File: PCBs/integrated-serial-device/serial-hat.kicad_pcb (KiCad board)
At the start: 2 copper layers, 193 x 113 mm, 28 parts, among them CN1 Modem port, CN2 Modem out 3, CN3 Printer port, J1 Rpi headers, K1 Quicktake, K2 ImageWriter, SW1 Modem To Proxy, SW2 Modem to Quicktake, SW3 Modem out 3, SW4 Printer out 3, SW5 Printer to Proxy, SW6 Printer to ImageWriter, U1 MAX3232

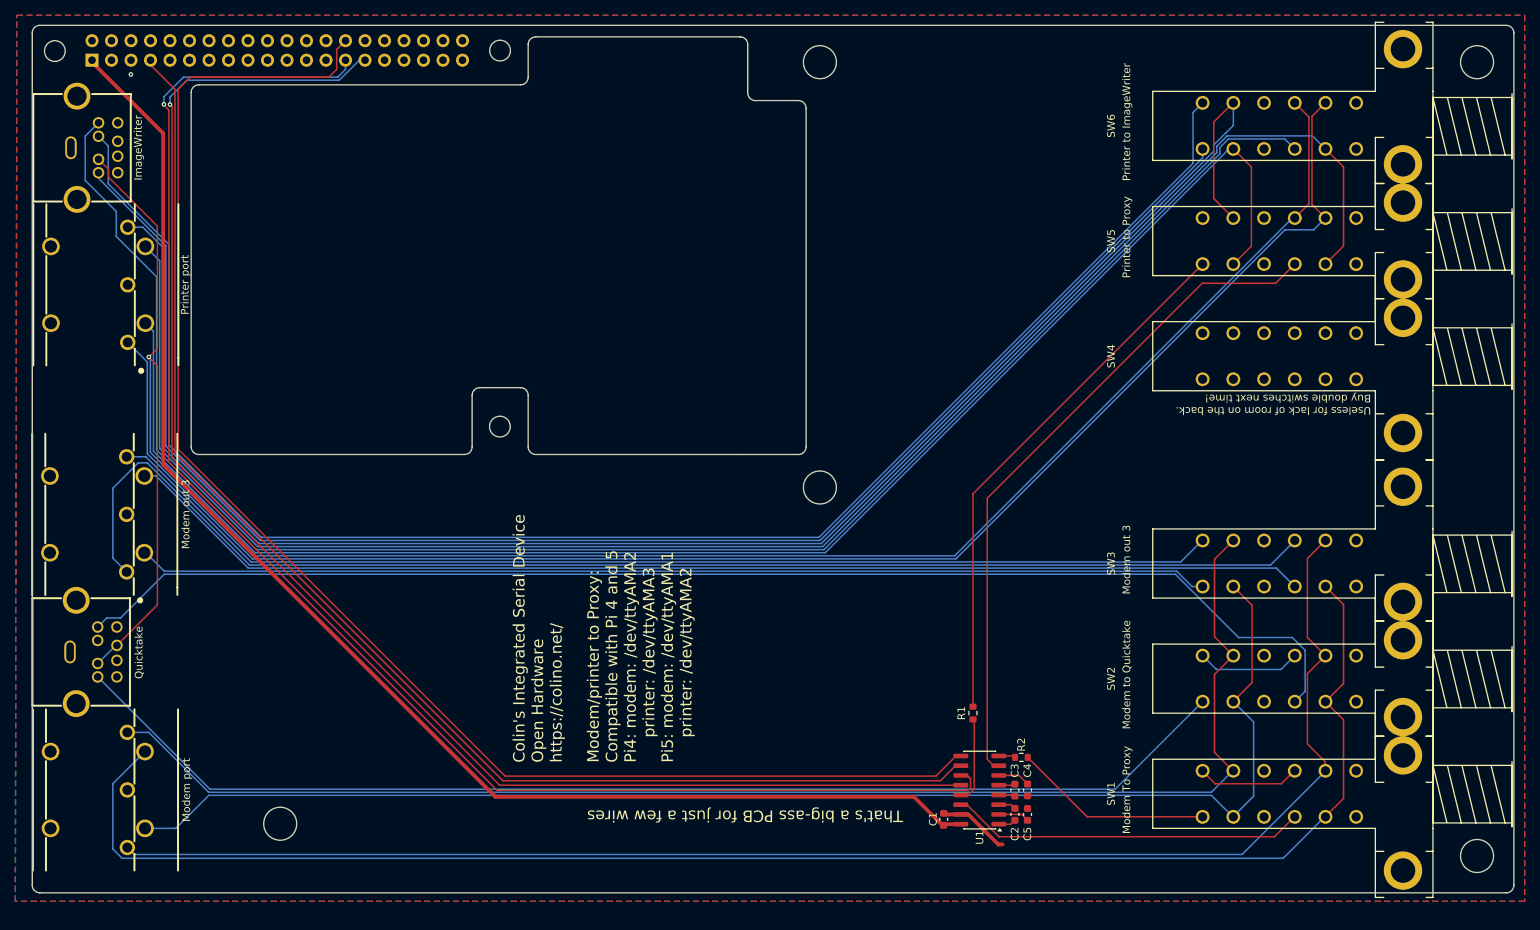
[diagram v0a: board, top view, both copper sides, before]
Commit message: Add jumper for IIc/IIgs
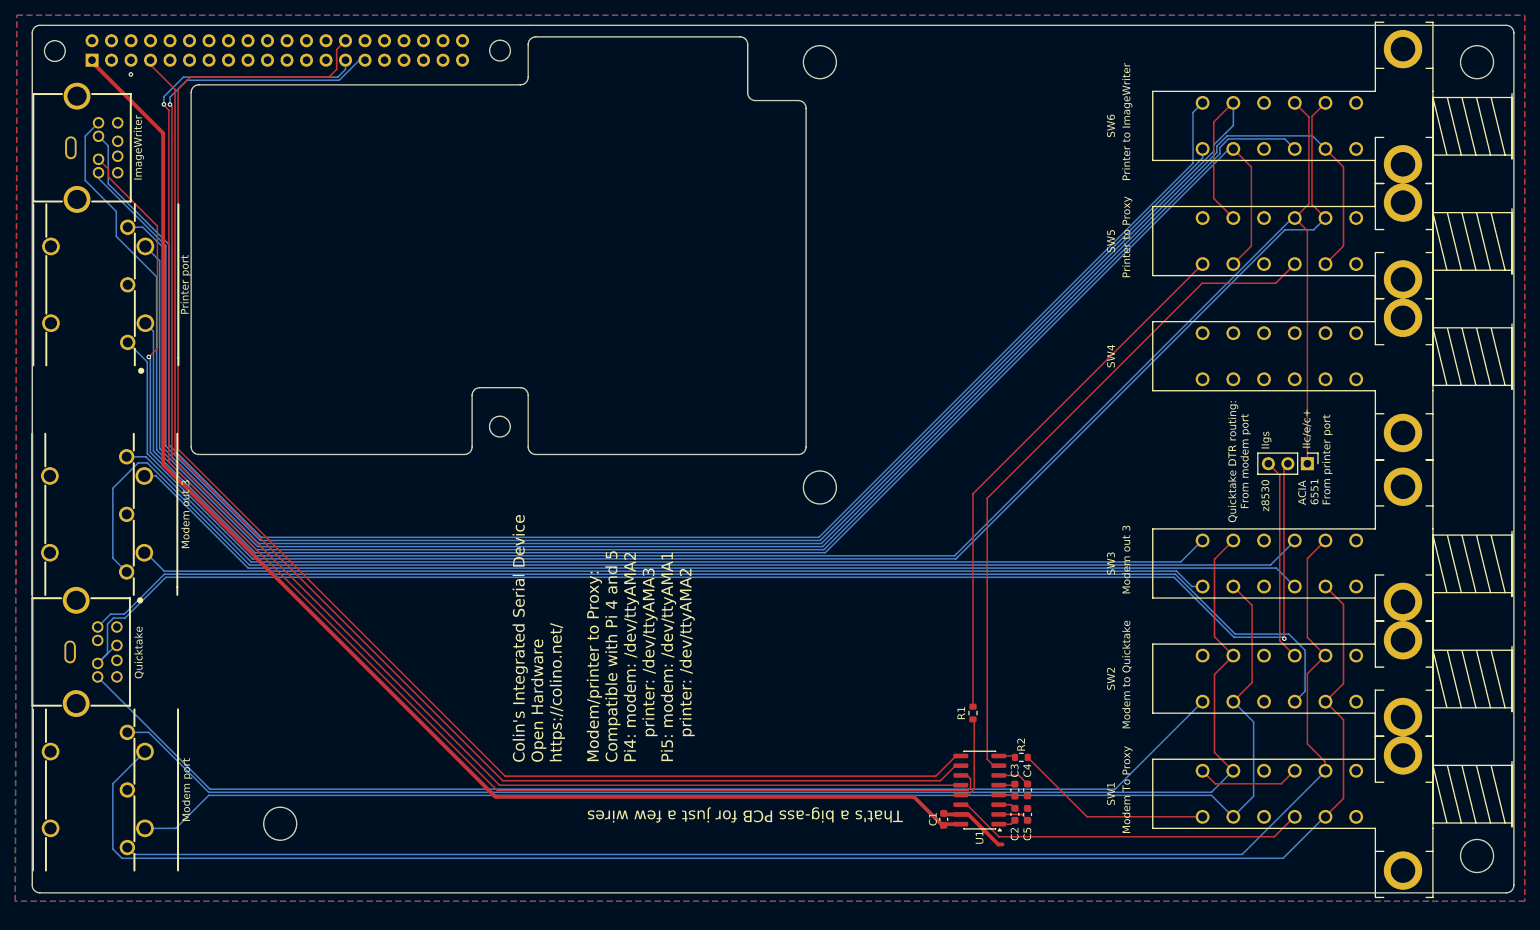
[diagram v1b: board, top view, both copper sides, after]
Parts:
- added J2: Conn_01x03_Pin, Connector_PinHeader_2.54mm:PinHeader_1x03_P2.54mm_Vertical, F.Cu at (219.9, 95.8)
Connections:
- K2 pad 1: Quicktake_DTR -> IW_DTR
- SW2 pad C1: Net-(SW2-PadC1) -> unconnected-(SW2-PadC1)
- SW2 pad D1: Net-(SW2-PadC1) -> Quicktake_DTR_Modem
- SW5 pad D1: Quicktake_DTR -> IW_DTR
- SW6 pad D1: Quicktake_DTR -> IW_DTR
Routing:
- net IW_DTR: track 0.00 -> 264.2 mm, vias 0 -> 1
- net Quicktake_DTR: track 275.2 -> 191.8 mm
- net Quicktake_DTR_Modem: track 0.00 -> 26.4 mm
- net Net-(SW2-PadC1): track 13.5 -> 0.00 mm
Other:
- board text added: "ACIA 6551"
- board text added: "From printer port"
- board text added: "IIc/e/c+"
- board text added: "IIgs"
- board text added: "Quicktake DTR routing: From modem port"
- board text added: "z8530"
- board text removed: "Useless for lack of room on the back. Buy double switches next time!"

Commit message: Add enclosures
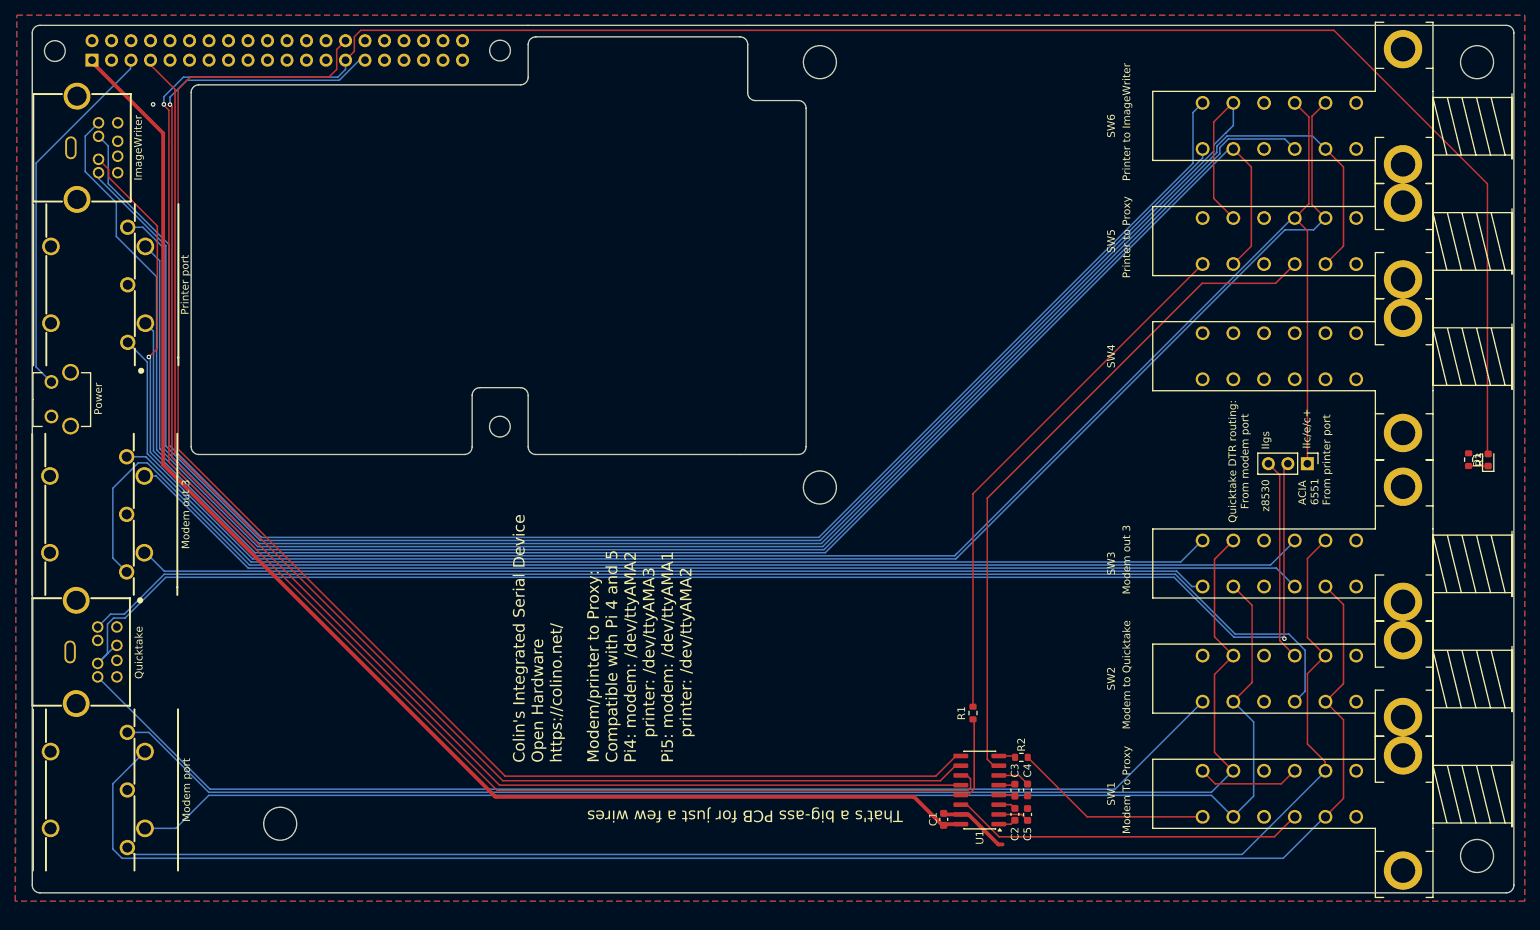
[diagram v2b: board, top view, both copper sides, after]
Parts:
- added D1: LED, LED_SMD:LED_0603_1608Metric, F.Cu at (243.4, 95.3)
- added R3: 100, Resistor_SMD:R_0603_1608Metric, F.Cu at (240.9, 95.3)
- added SW7: SW_SPST, DIN5:SPST_power_switch, F.Cu at (58.9, 87.5)
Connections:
- net TX0_out_GPIO0 renamed PWR_LED
- J1 pad 5: unconnected-(J1-Pin_5-Pad5) -> PWR_BTN
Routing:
- net PWR_LED: track 199.1 -> 394.1 mm
- net PWR_BTN: track 0.00 -> 47.9 mm
- net Net-(D1-K): track 0.00 -> 2.55 mm
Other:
- board text added: "Power"

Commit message: Add fan headers
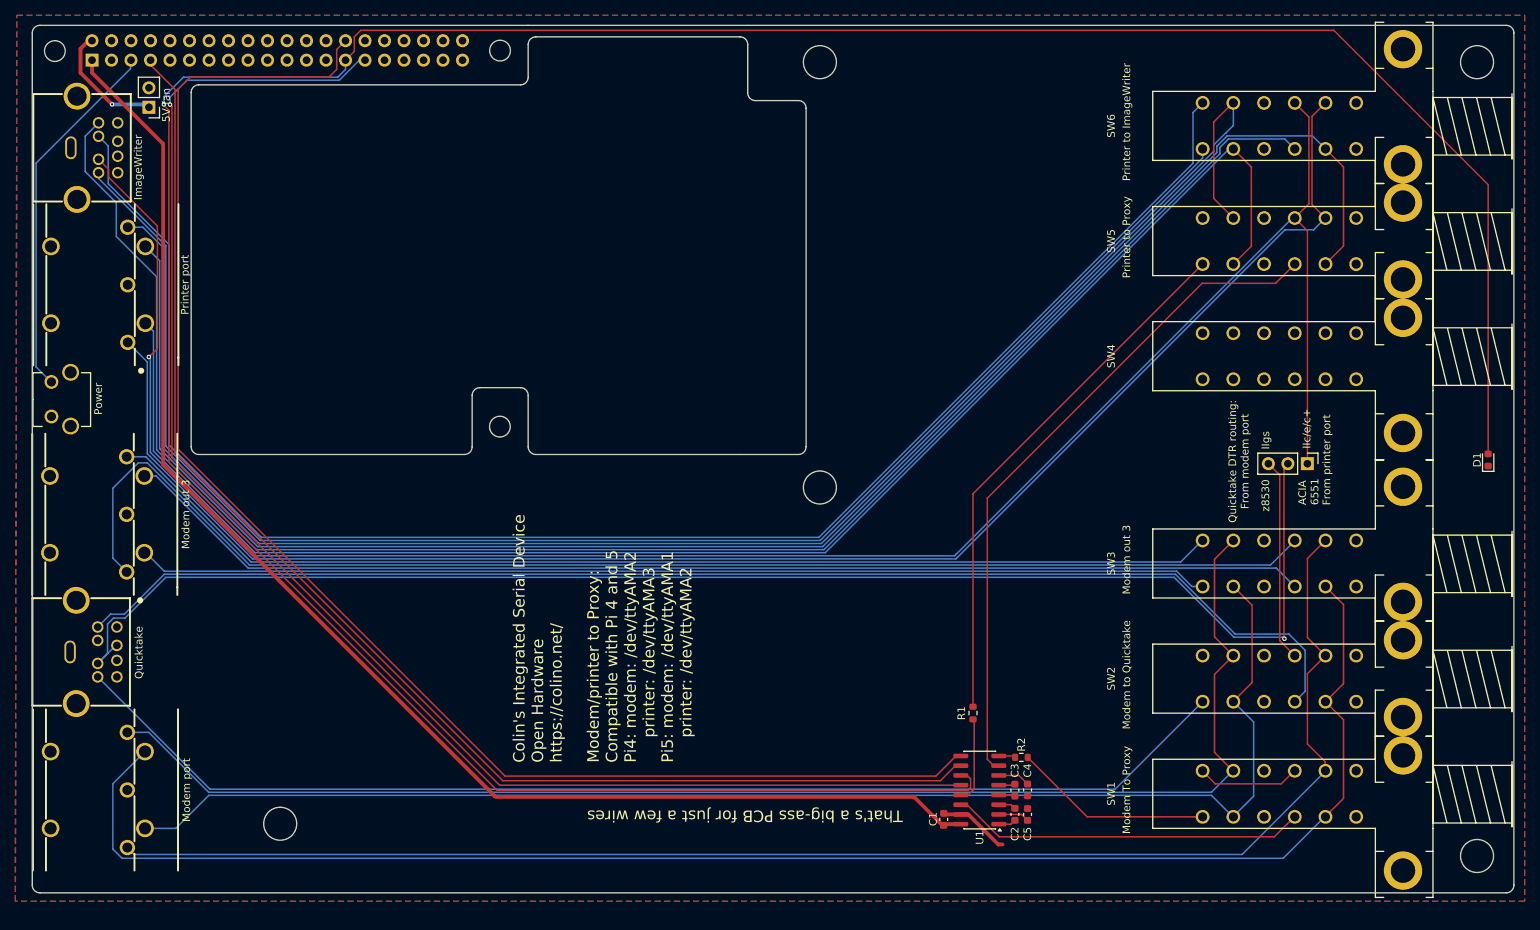
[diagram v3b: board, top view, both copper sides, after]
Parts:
- removed R3: 100, Resistor_SMD:R_0603_1608Metric
- added J3: Conn_01x02_Pin, Connector_PinHeader_2.54mm:PinHeader_1x02_P2.54mm_Vertical, F.Cu at (69.0, 49.4)
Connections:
- D1 pad 1: Net-(D1-K) -> GND
- J1 pad 2: unconnected-(J1-Pin_2-Pad2) -> 5V
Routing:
- net 5V: track 0.00 -> 15.8 mm, vias 0 -> 1
- net Net-(D1-K): track 2.55 -> 0.00 mm
- net GND: vias 1 -> 0
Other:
- board text added: "5V fan"

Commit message: CISD ready
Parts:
- removed R1, R2: 3.3k, Resistor_SMD:R_0603_1608Metric
- moved J3 2.68 mm to (69.0, 46.7), turned to 0 degrees
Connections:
- U1 pad 13: Net-(U1-R1IN) -> A2_AUX_TTY_TX
- U1 pad 8: Net-(U1-R2IN) -> A2_TTY_TX
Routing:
- net A2_AUX_TTY_TX: track 70.2 -> 82.8 mm
- net Net-(U1-R1IN): track 11.2 -> 0.00 mm
- net GND: track 9.35 -> 16.7 mm
- net A2_TTY_TX: track 25.9 -> 29.8 mm
- net Net-(U1-R2IN): track 2.20 -> 0.00 mm
- net 5V: track 15.8 -> 16.6 mm

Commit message: Fix CISD Quicktake
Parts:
- removed J2: Conn_01x03_Pin, Connector_PinHeader_2.54mm:PinHeader_1x03_P2.54mm_Vertical
- removed MH6: MountingHole_4.3mm_M4, MountingHole:MountingHole_4.3mm_M4
- added SW8: SW_Slide_DPDT, DIN5:DPDT slide switch C7507433, F.Cu at (91.1, 150.8)
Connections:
- K1 pad 2: unconnected-(K1-Pad2) -> Quicktake_DSR
- SW2 pad C1: unconnected-(SW2-PadC1) -> Quicktake_DSR_Modem
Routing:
- net IW_DTR: track 264.2 -> 443.1 mm
- net Quicktake_DSR_Modem: track 0.00 -> 167.0 mm
- net Quicktake_DTR: track 191.8 -> 47.7 mm, vias 1 -> 0
- net Quicktake_DTR_Modem: track 26.4 -> 163.0 mm
- net Quicktake_DSR: track 0.00 -> 47.5 mm
- net Quicktake_TX: track 171.5 -> 173.7 mm
- net Modem_DTR_in: track 194.8 -> 196.6 mm
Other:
- board text removed: "ACIA 6551"
- board text removed: "From printer port"
- board text removed: "Quicktake DTR routing: From modem port"
- board text removed: "z8530"

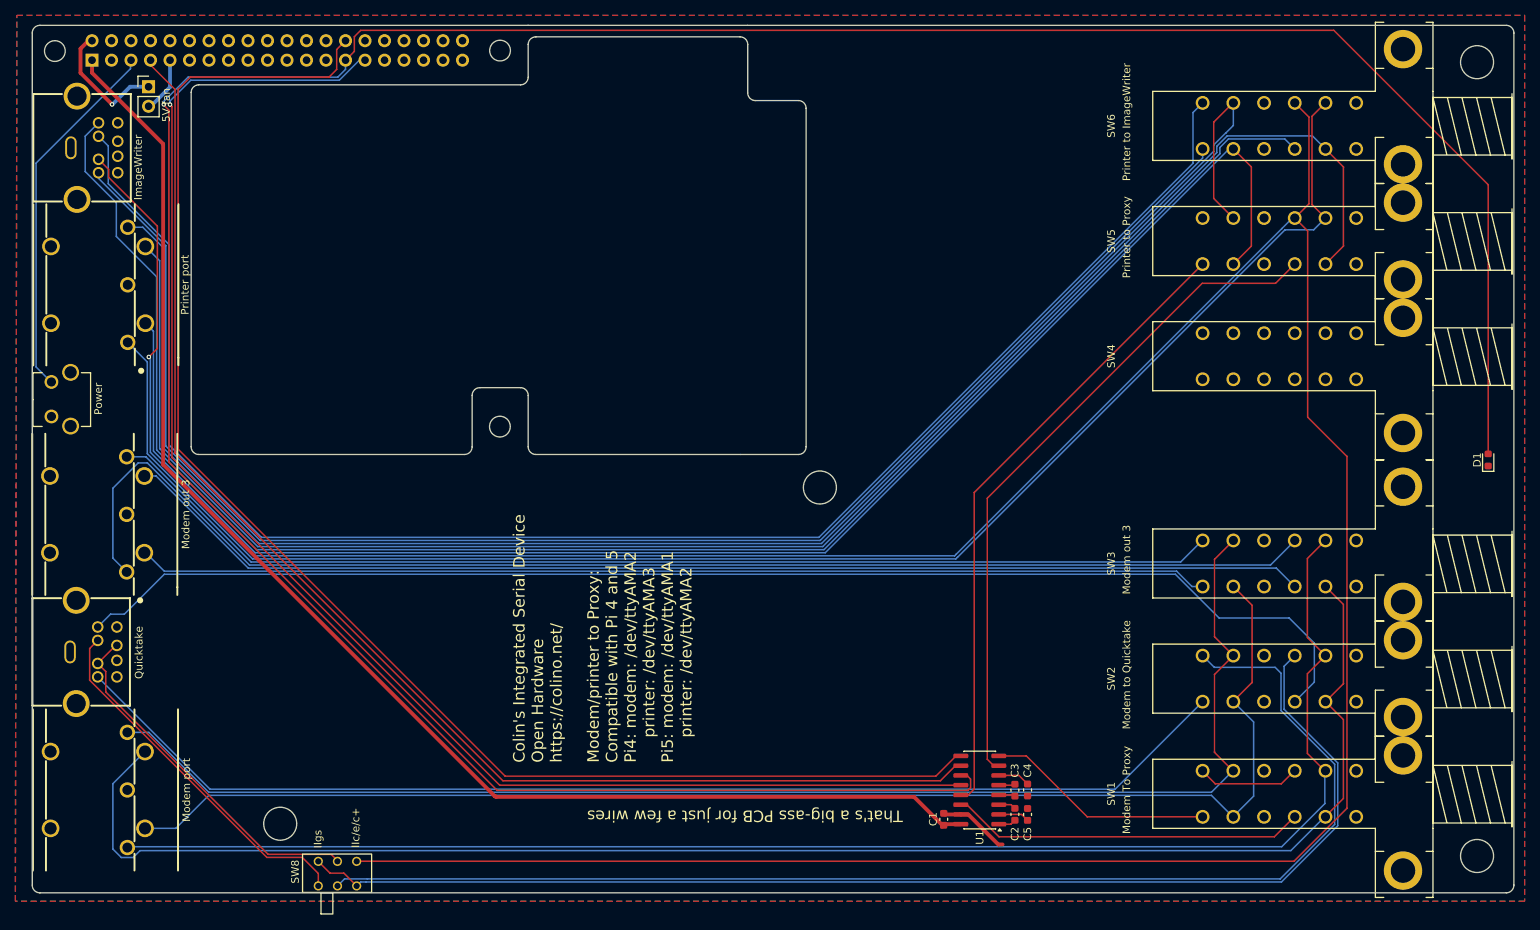
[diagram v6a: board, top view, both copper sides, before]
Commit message: Add references
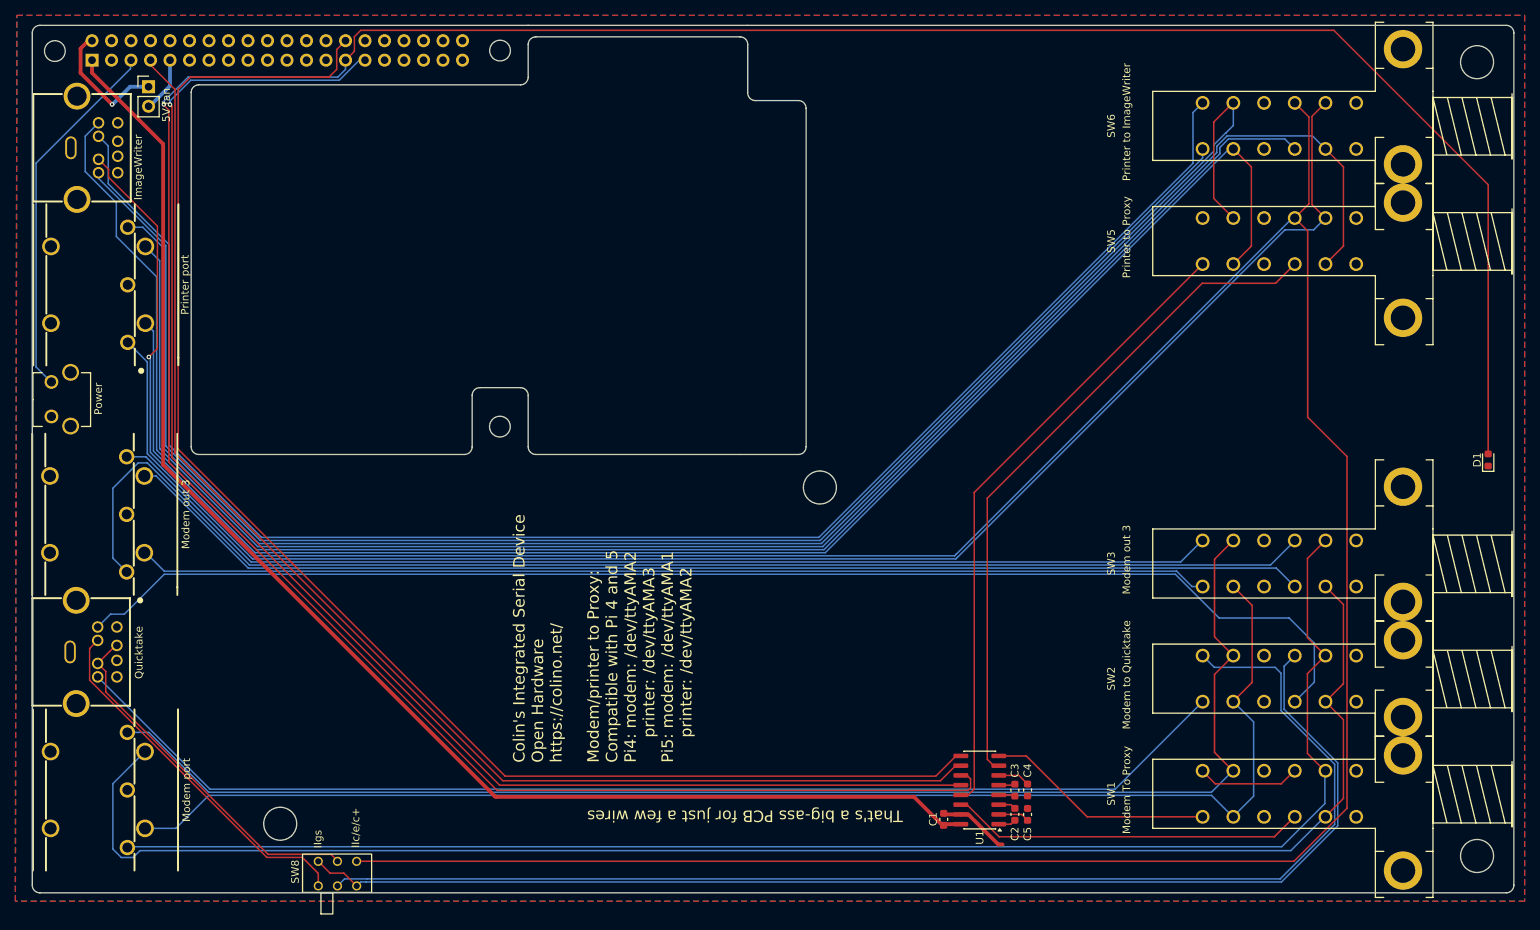
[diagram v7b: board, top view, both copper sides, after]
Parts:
- removed SW4: Printer out 3, DIN5:4PDT piano switch
- SW8: value SW_Slide_DPDT -> SW_Slide_DPDT SHOU HAN MSK-22D18G4 051
